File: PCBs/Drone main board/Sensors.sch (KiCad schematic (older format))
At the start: 29 parts, among them U701 ICM-20602, U702 TXB0108PWR, U703 BNO055, U704 DPS422XTSA1, U705 MCP3208, Y701 32.7KHz

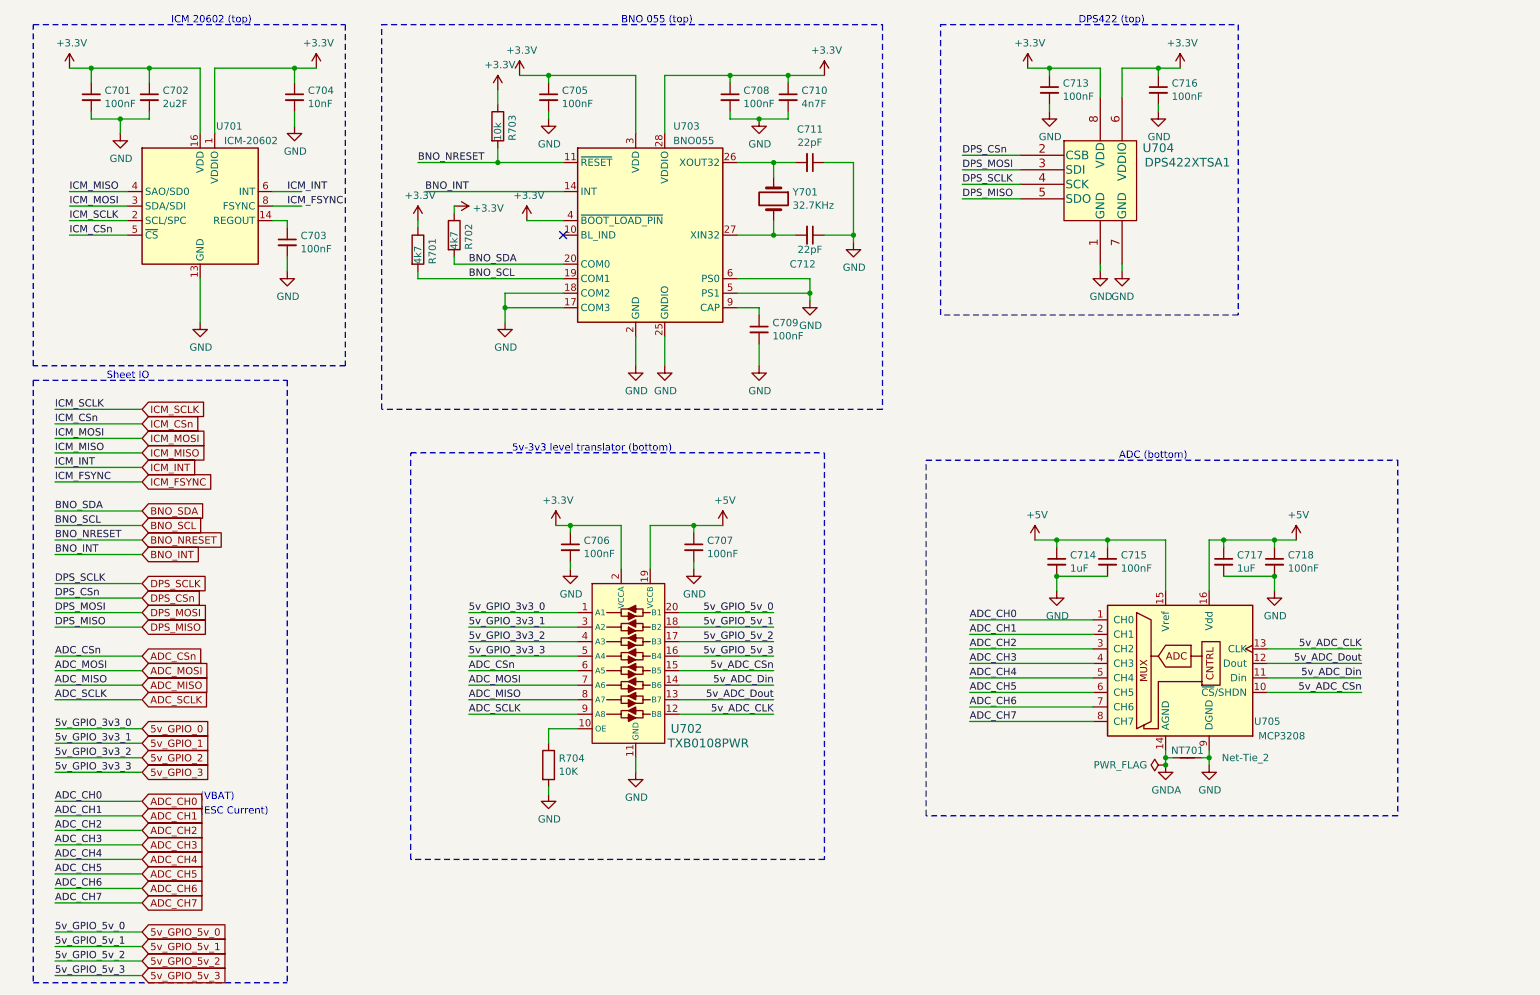
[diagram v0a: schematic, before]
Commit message: Added PDFs of schematics. Corrected a few value labels in drone schematic.
Signed-off-by: Eldalote.Electronics <Eldalote.Electronics@gmail.com>
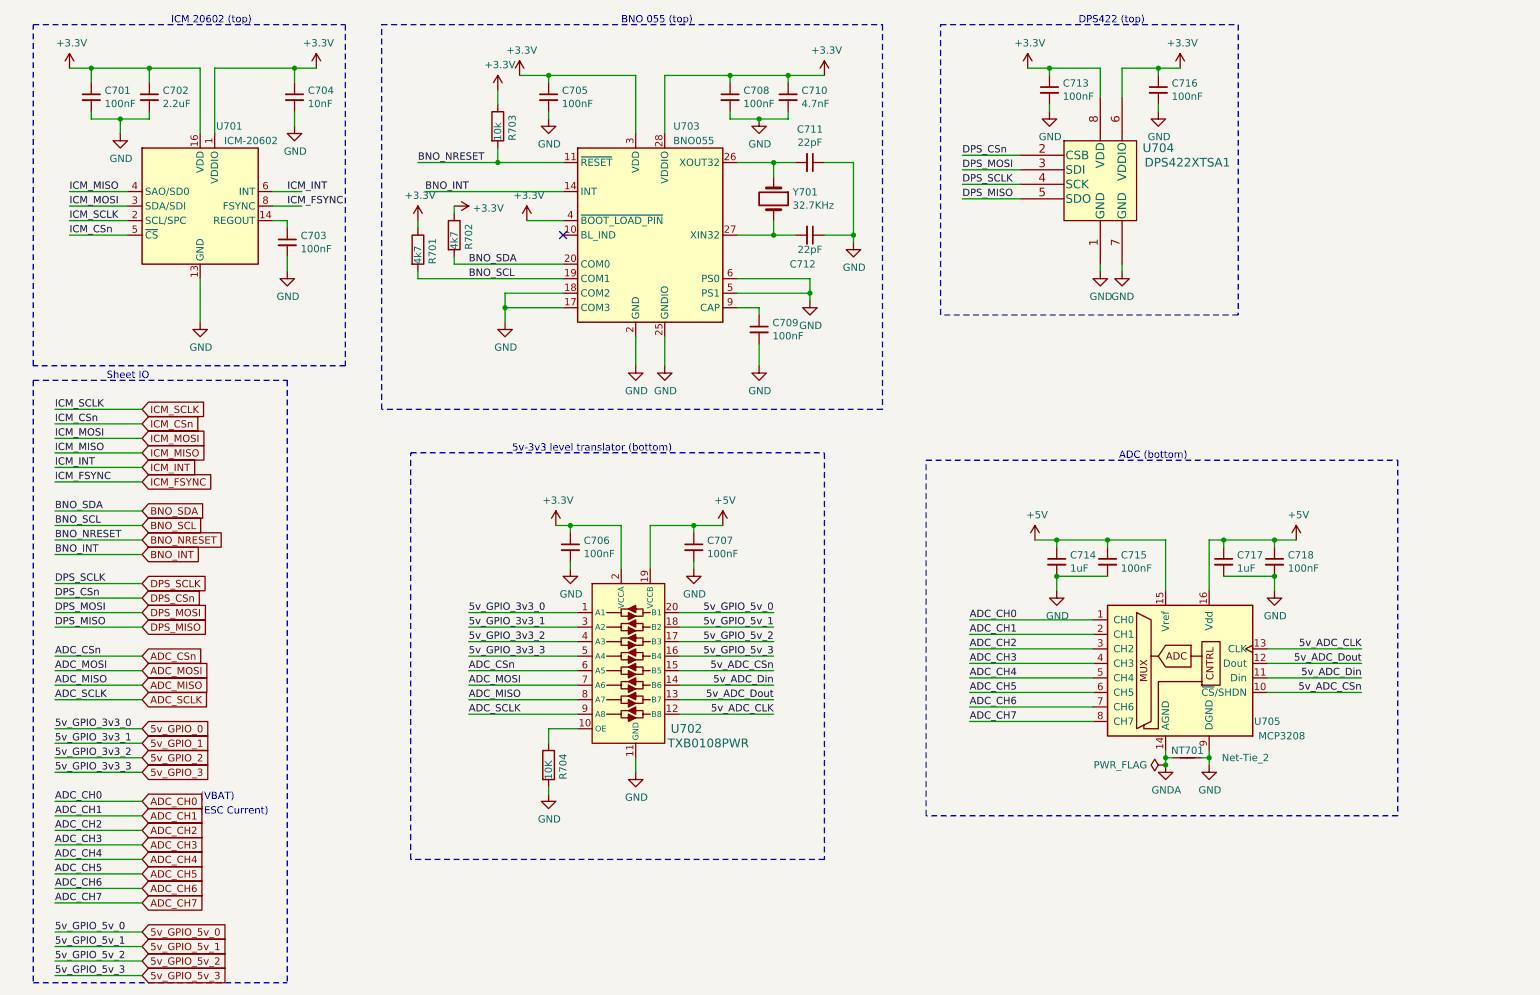
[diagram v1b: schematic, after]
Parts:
- C702: value 2u2F -> 2.2uF
- C710: value 4n7F -> 4.7nF
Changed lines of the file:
@@
 P 1550 1100
 F 0 "C702" H 1642 1146 50  0000 L CNN
-F 1 "2u2F" H 1642 1055 50  0000 L CNN
+F 1 "2.2uF" H 1642 1055 50  0000 L CNN
 F 2 "Capacitor_SMD:C_0603_1608Metric" H 1550 1100 50  0001 C CNN
 F 3 "~" H 1550 1100 50  0001 C CNN
@@
 P 5950 1100
 F 0 "C710" H 6042 1146 50  0000 L CNN
-F 1 "4n7F" H 6042 1055 50  0000 L CNN
+F 1 "4.7nF" H 6042 1055 50  0000 L CNN
 F 2 "Capacitor_SMD:C_0603_1608Metric" H 5950 1100 50  0001 C CNN
 F 3 "~" H 5950 1100 50  0001 C CNN
@@
 U 1 1 5F81452C
 P 4300 5700
-F 0 "R704" H 4370 5746 50  0000 L CNN
-F 1 "10K" H 4370 5655 50  0000 L CNN
+F 0 "R704" V 4400 5600 50  0000 L CNN
+F 1 "10K" V 4300 5600 50  0000 L CNN
 F 2 "Resistor_SMD:R_0805_2012Metric_Pad1.15x1.40mm_HandSolder" V 4230 5700 50  0001 C CNN
 F 3 "~" H 4300 5700 50  0001 C CNN

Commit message: Lots of work to check every component, add Manufacturers number (instead of LCSC or digikey and mouser numbers)
Changed to USB-C connector, almost done with that sheet. Components checked, need to redo Sheet IO

Signed-off-by: Eldalote.Electronics <Eldalote.Electronics@gmail.com>
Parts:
- C701, C703, C705, C708, C709, C713, C716: LCSC C1525 -> (none); MfNr (none) -> CL05B104KO5NNNC
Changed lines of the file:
@@
 F 2 "Capacitor_SMD:C_0402_1005Metric" H 1150 1100 50  0001 C CNN
 F 3 "~" H 1150 1100 50  0001 C CNN
-F 4 "C1525" H 1150 1100 50  0001 C CNN "LCSC"
+F 4 "" H 1150 1100 50  0001 C CNN "LCSC"
+F 5 "CL05B104KO5NNNC" H 1150 1100 50  0001 C CNN "MfNr"
 	1    1150 1100
 	1    0    0    -1
@@
 F 2 "Capacitor_SMD:C_0402_1005Metric" H 2500 2100 50  0001 C CNN
 F 3 "~" H 2500 2100 50  0001 C CNN
-F 4 "C1525" H 2500 2100 50  0001 C CNN "LCSC"
+F 4 "" H 2500 2100 50  0001 C CNN "LCSC"
+F 5 "CL05B104KO5NNNC" H 2500 2100 50  0001 C CNN "MfNr"
 	1    2500 2100
 	1    0    0    -1
@@
 F 2 "Capacitor_SMD:C_0402_1005Metric" H 4300 1100 50  0001 C CNN
 F 3 "~" H 4300 1100 50  0001 C CNN
-F 4 "C1525" H 4300 1100 50  0001 C CNN "LCSC"
+F 4 "" H 4300 1100 50  0001 C CNN "LCSC"
+F 5 "CL05B104KO5NNNC" H 4300 1100 50  0001 C CNN "MfNr"
 	1    4300 1100
 	1    0    0    -1
@@
 F 2 "Capacitor_SMD:C_0402_1005Metric" H 5550 1100 50  0001 C CNN
 F 3 "~" H 5550 1100 50  0001 C CNN
-F 4 "C1525" H 5550 1100 50  0001 C CNN "LCSC"
+F 4 "" H 5550 1100 50  0001 C CNN "LCSC"
+F 5 "CL05B104KO5NNNC" H 5550 1100 50  0001 C CNN "MfNr"
 	1    5550 1100
 	1    0    0    -1
@@
 F 2 "Capacitor_SMD:C_0402_1005Metric" H 5750 2700 50  0001 C CNN
 F 3 "~" H 5750 2700 50  0001 C CNN
-F 4 "C1525" H 5750 2700 50  0001 C CNN "LCSC"
+F 4 "" H 5750 2700 50  0001 C CNN "LCSC"
+F 5 "CL05B104KO5NNNC" H 5750 2700 50  0001 C CNN "MfNr"
 	1    5750 2700
 	1    0    0    -1
@@
 F 2 "Capacitor_SMD:C_0402_1005Metric" H 7750 1050 50  0001 C CNN
 F 3 "~" H 7750 1050 50  0001 C CNN
-F 4 "C1525" H 7750 1050 50  0001 C CNN "LCSC"
+F 4 "" H 7750 1050 50  0001 C CNN "LCSC"
+F 5 "CL05B104KO5NNNC" H 7750 1050 50  0001 C CNN "MfNr"
 	1    7750 1050
 	1    0    0    -1
@@
 F 2 "Capacitor_SMD:C_0402_1005Metric" H 8500 1050 50  0001 C CNN
 F 3 "~" H 8500 1050 50  0001 C CNN
-F 4 "C1525" H 8500 1050 50  0001 C CNN "LCSC"
+F 4 "" H 8500 1050 50  0001 C CNN "LCSC"
+F 5 "CL05B104KO5NNNC" H 8500 1050 50  0001 C CNN "MfNr"
 	1    8500 1050
 	1    0    0    -1

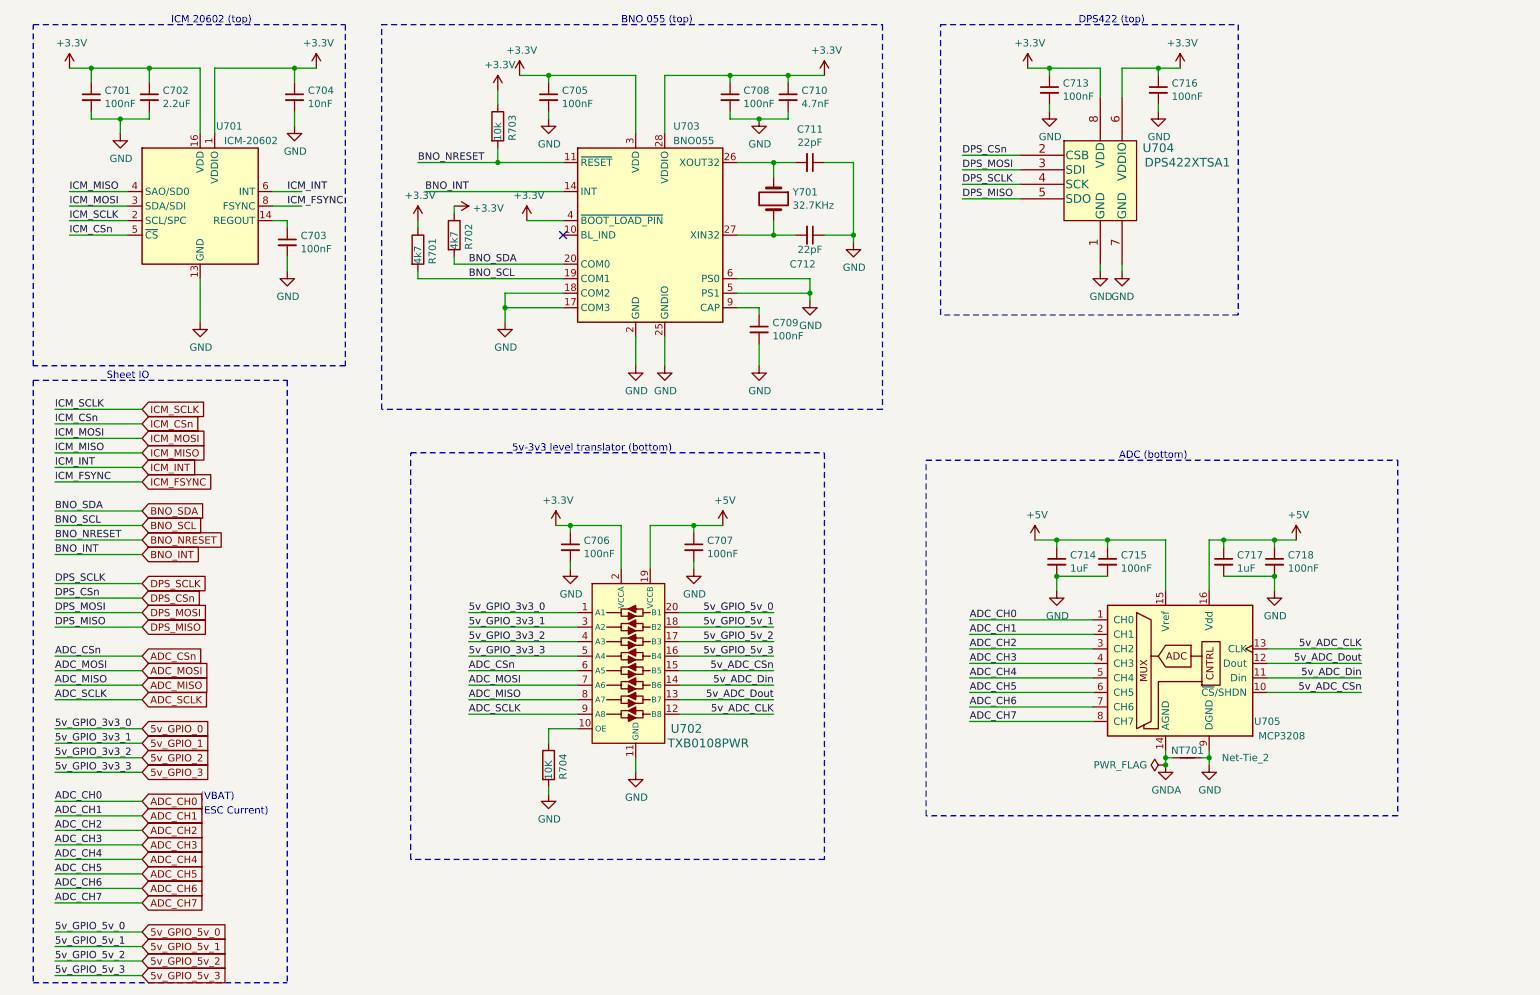
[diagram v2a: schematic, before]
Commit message: Reworking and checking up to sensors page on main board. Added some datasheets to project
Signed-off-by: Eldalote.Electronics <Eldalote.Electronics@gmail.com>
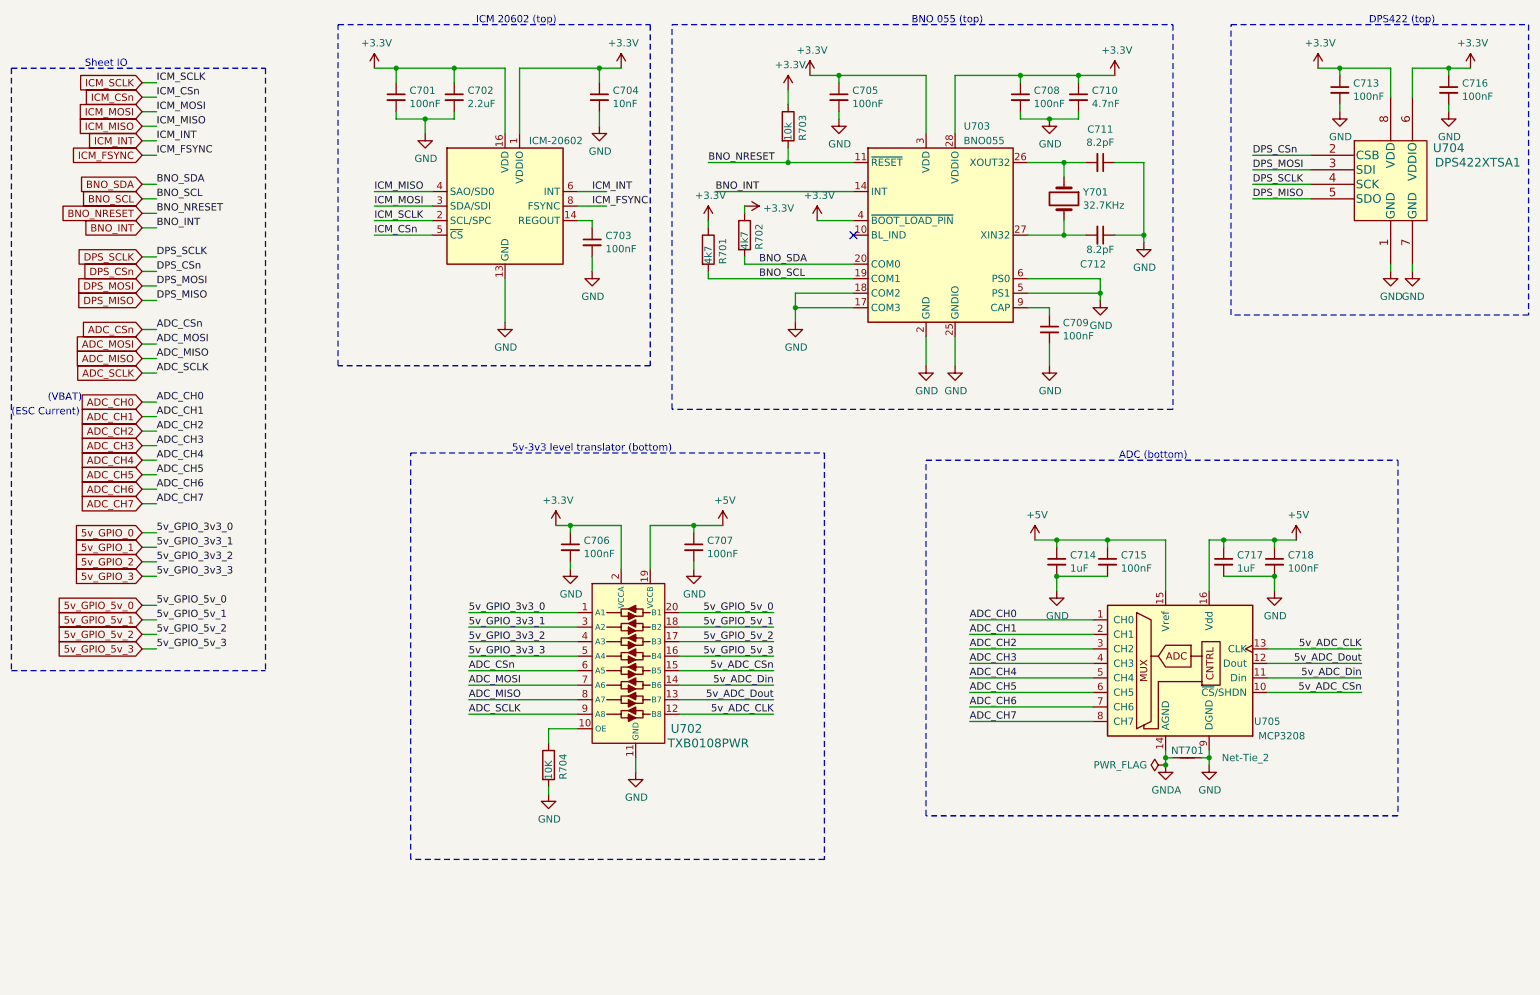
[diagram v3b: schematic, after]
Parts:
- C702: LCSC C23630 -> (none); MfNr (none) -> CL10A225KO8NNN
- C704: LCSC C15195 -> (none); MfNr (none) -> CL05B103KB5NNN
- C706, C707, C715, C718: footprint Capacitor_SMD:C_0805_2012Metric_Pad1.15x1.40mm_HandSolder -> Capacitor_SMD:C_0402_1005Metric; DigiKey 1276-1099-1-ND -> (none); MfNr (none) -> CL05B104KO5NNNC; Mouser 187-CL21B104KACNNNC -> (none)
- C710: footprint Capacitor_SMD:C_0603_1608Metric -> Capacitor_SMD:C_0402_1005Metric; LCSC C53987 -> (none); MfNr (none) -> CC0402KRX7R9BB472
- C711, C712: value 22pF -> 8.2pF; footprint Capacitor_SMD:C_0603_1608Metric -> Capacitor_SMD:C_0402_1005Metric; LCSC C1653 -> (none); MfNr (none) -> CC0402CRNPO9BN8R2
- C714: footprint Capacitor_SMD:C_0805_2012Metric_Pad1.15x1.40mm_HandSolder -> Capacitor_SMD:C_0603_1608Metric; DigiKey 1276-1066-1-ND -> (none); MfNr (none) -> CL10A105KB8NNNC; Mouser 187-CL21B105KAFNNNE -> (none)
- C717: footprint Capacitor_SMD:C_0805_2012Metric_Pad1.15x1.40mm_HandSolder -> Capacitor_SMD:C_0603_1608Metric; DigiKey 1276-1066-1-ND -> (none); Mouser 187-CL21B105KAFNNNE -> CL10A105KB8NNNC
- R701, R702: LCSC C25900 -> (none); MfNr (none) -> RC0402FR-074K7L
- R703: LCSC C25744 -> (none); MfNr (none) -> RC0402FR-0710KL
- R704: footprint Resistor_SMD:R_0805_2012Metric_Pad1.15x1.40mm_HandSolder -> Resistor_SMD:R_0402_1005Metric; DigiKey 311-10.0KCRCT-ND -> (none); MfNr (none) -> RC0402FR-0710KL; Mouser 603-RC0805FR-0710KL -> (none)
- U701: DigiKey 1428-1060-1-ND -> (none); MfNr (none) -> ICM-20602; Mouser 410-ICM-20602 -> (none)
- U702: Digi-Key_PN 296-21527-1-ND -> (none); MPN TXB0108PWR -> (none); MfNr (none) -> TXB0108PWR
- U704: DigiKey DPS422XTSA1CT-ND -> (none); MfNr (none) -> DPS422XTSA1; Mouser 726-DPS422XTSA1 -> (none)
- U705: DigiKey MCP3208-CI/SL-ND -> (none); MfNr (none) -> MCP3208-CI/SL; Mouser 579-MCP3208CISL -> (none)
- Y701: LCSC C32346 -> (none); MfNr (none) -> NX3215SA-32.768K-STD-MUA-9
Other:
- moved on the sheet: C701, C702, C703, C704, C705, C708, C709, C710, C711, C712, C713, C716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

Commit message: Finished (?) the schematic check and update. Next: PCB update
Signed-off-by: Eldalote.Electronics <Eldalote.Electronics@gmail.com>
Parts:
- C717: MfNr (none) -> CL10A105KB8NNNC; Mouser CL10A105KB8NNNC -> (none)
- U703: DigiKey 828-1058-1-ND -> (none); MfNr (none) -> BNO055; Mouser 262-BNO055 -> (none)
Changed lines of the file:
@@
 F 2 "Package_LGA:LGA-28_5.2x3.8mm_P0.5mm" H 7250 1400 50  0001 L CNN
 F 3 "https://ae-bst.resource.bosch.com/media/_tech/media/datasheets/BST_BNO055_DS000_14.pdf" H 7000 2250 50  0001 C CNN
-F 4 "828-1058-1-ND" H 7000 2050 50  0001 C CNN "DigiKey"
-F 5 "262-BNO055 " H 7000 2050 50  0001 C CNN "Mouser"
+F 4 "" H 7000 2050 50  0001 C CNN "DigiKey"
+F 5 "" H 7000 2050 50  0001 C CNN "Mouser"
+F 6 "BNO055" H 7000 2050 50  0001 C CNN "MfNr"
 	1    7000 2050
 	1    0    0    -1
@@
 F 2 "Capacitor_SMD:C_0603_1608Metric" H 8950 4300 50  0001 C CNN
 F 3 "~" H 8950 4300 50  0001 C CNN
-F 4 "CL10A105KB8NNNC" H 8950 4300 50  0001 C CNN "Mouser"
+F 4 "CL10A105KB8NNNC" H 8950 4300 50  0001 C CNN "MfNr"
 	1    8950 4300
 	1    0    0    -1
